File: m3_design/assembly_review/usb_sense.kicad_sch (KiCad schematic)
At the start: 3 parts

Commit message: R2 part-by-part datasheet verification; fix every issue found
All 99 BOM lines / 205 positions checked against manufacturer datasheets
(pinout, land pattern, polarity, part number, 3D orientation); record in
docs/R2_VERIFICATION.md.

Fixes:
- R134/R135: Bourns CRM2512 recommended land (2.45 x 3.7 mm pads, 7.6 mm),
  moved to keep clearance; generic 2512 land had ~45 % of the pad area.
- BOOT0 rerouted out from between the MS5611 pads (TE: do not route
  between pads); 0/45/90 segments instead of 0.1 mm staircases.
- C84 polarity mark on the top side; U12 pin-1 mark.
- AON7524 3D model rotated 180 deg; L1/L2 model height 3.0 mm.
- R84 C705743, R9 C25915, R86 80.6k 0.1% C861568 (80k not orderable);
  every BOM line now has an LCSC code.
- sim_r2: fire with all four servos stalled (FMEA V-15) passes.
- FMEA H-1..H-10 status, redundancy table, firmware requirements,
  README / STATUS / AGENTS updated for R2.

DRC 0 / unconnected 0 / parity 0 / ERC 0, audit OK, actuator contract OK;
diagnostics 173, firmware 112, quality_audit 12 tests pass; sim 135 PASS.

Co-Authored-By: Claude Opus 5.5 (1M context) <noreply@anthropic.com>
Claude-Session: https://claude.ai/code/session_01DdkfTxR7SVyv9xZNmPk9vB
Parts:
- R9: LCSC (none) -> C25915; LCSC Part (none) -> C25915; Manufacturer Yageo -> UNI-ROYAL; Manufacturer Part RC0402FR-076K2L -> 0402WGF6201TCE
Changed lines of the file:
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@@
 					(size 1.27 1.27))
 				(justify left)))
-		(property "LCSC" ""
+		(property "LCSC" "C25915"
 			(at 78.74 83.82 0)
 			(hide yes)
@@
 					(reference "R9")
 					(unit 1))))
-		(property "Manufacturer" "Yageo"
+		(property "Manufacturer" "UNI-ROYAL"
 			(at 78.74 83.82 0)
 			(hide yes)
@@
 				(font
 					(size 1.27 1.27))))
-		(property "Manufacturer Part" "RC0402FR-076K2L"
+		(property "Manufacturer Part" "0402WGF6201TCE"
 			(at 78.74 83.82 0)
 			(hide yes)
@@
 				(font
 					(size 1.27 1.27))))
-		(property "LCSC Part" ""
+		(property "LCSC Part" "C25915"
 			(at 78.74 83.82 0)
 			(hide yes)

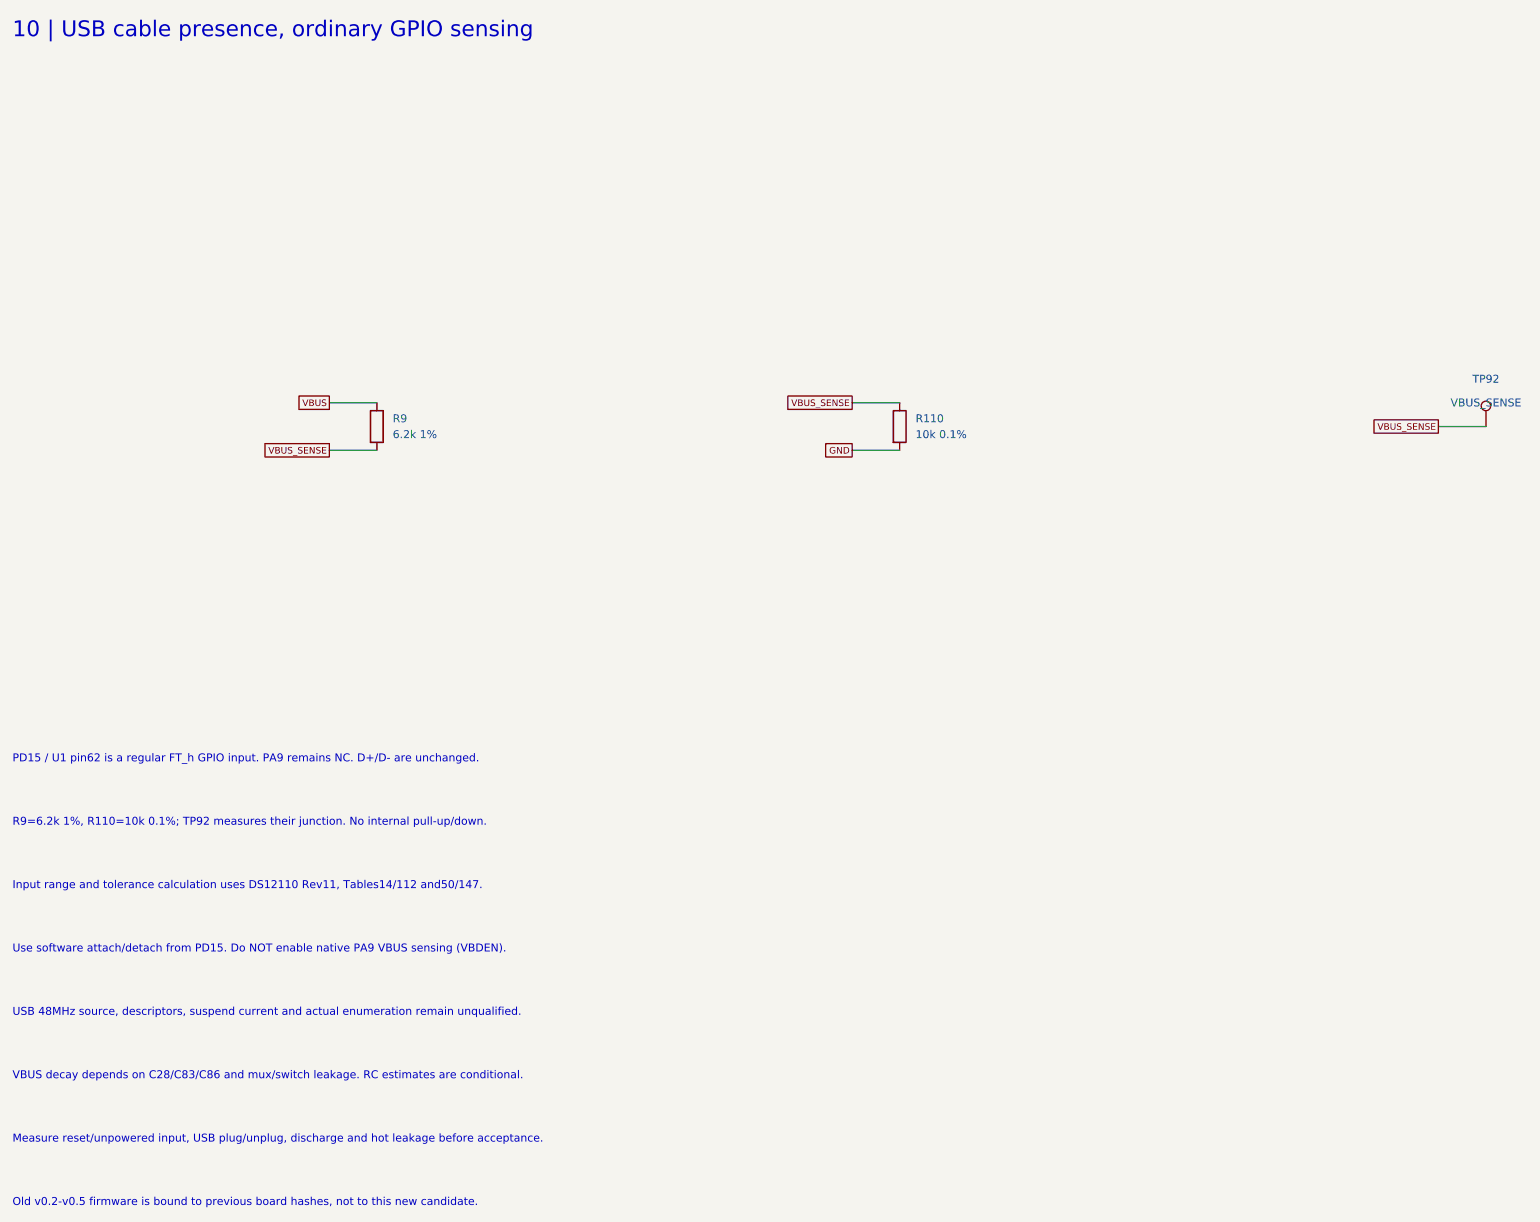
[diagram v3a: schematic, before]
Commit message: M3-ASSY-R4: R3 validation fixes, new IMU, fault-tolerant pyro sensing
The board, schematic sheets and footprint library are generated from
R3 (533af8e) by m3_design/r4_build.sh (r4_lib.py, r4_sch.py,
r4_pcb.py). docs/REQUIREMENTS.md states what the board must do;
docs/M3_R4.md records every change, the thirteen evaluation passes
(twelve independent reviews) and the accepted deviations.

- IMU: ST LSM6DSV320X (16 g and 320 g, 4000 dps)
- Pyro: black ARM and orange igniter terminals, eight pyro spacing
  rules in m3.kicad_dru, sense dividers of 2 x 5.1k over 2 x 2k in
  parallel, 4.7k at each ADC pin (R168-R172)
- Pull-pin on a JST PH connector; JLC tooling holes
- Fab: Standard PCBA, 84 BOM lines, 205 placed parts, $80.12 per board
  at five boards (tools/jlc_cost.py); placement rotations verified
- Gate: tools/check.sh DRC 0, unconnected 0, schematic parity 0, ERC 0,
  audit OK; m3_design/check_actuators.py OK

Nothing has been built or measured, and there is no R4 firmware. The
open owner decisions and the bench tests are listed in STATUS.md.

Co-Authored-By: Claude Opus 5.5 <noreply@anthropic.com>
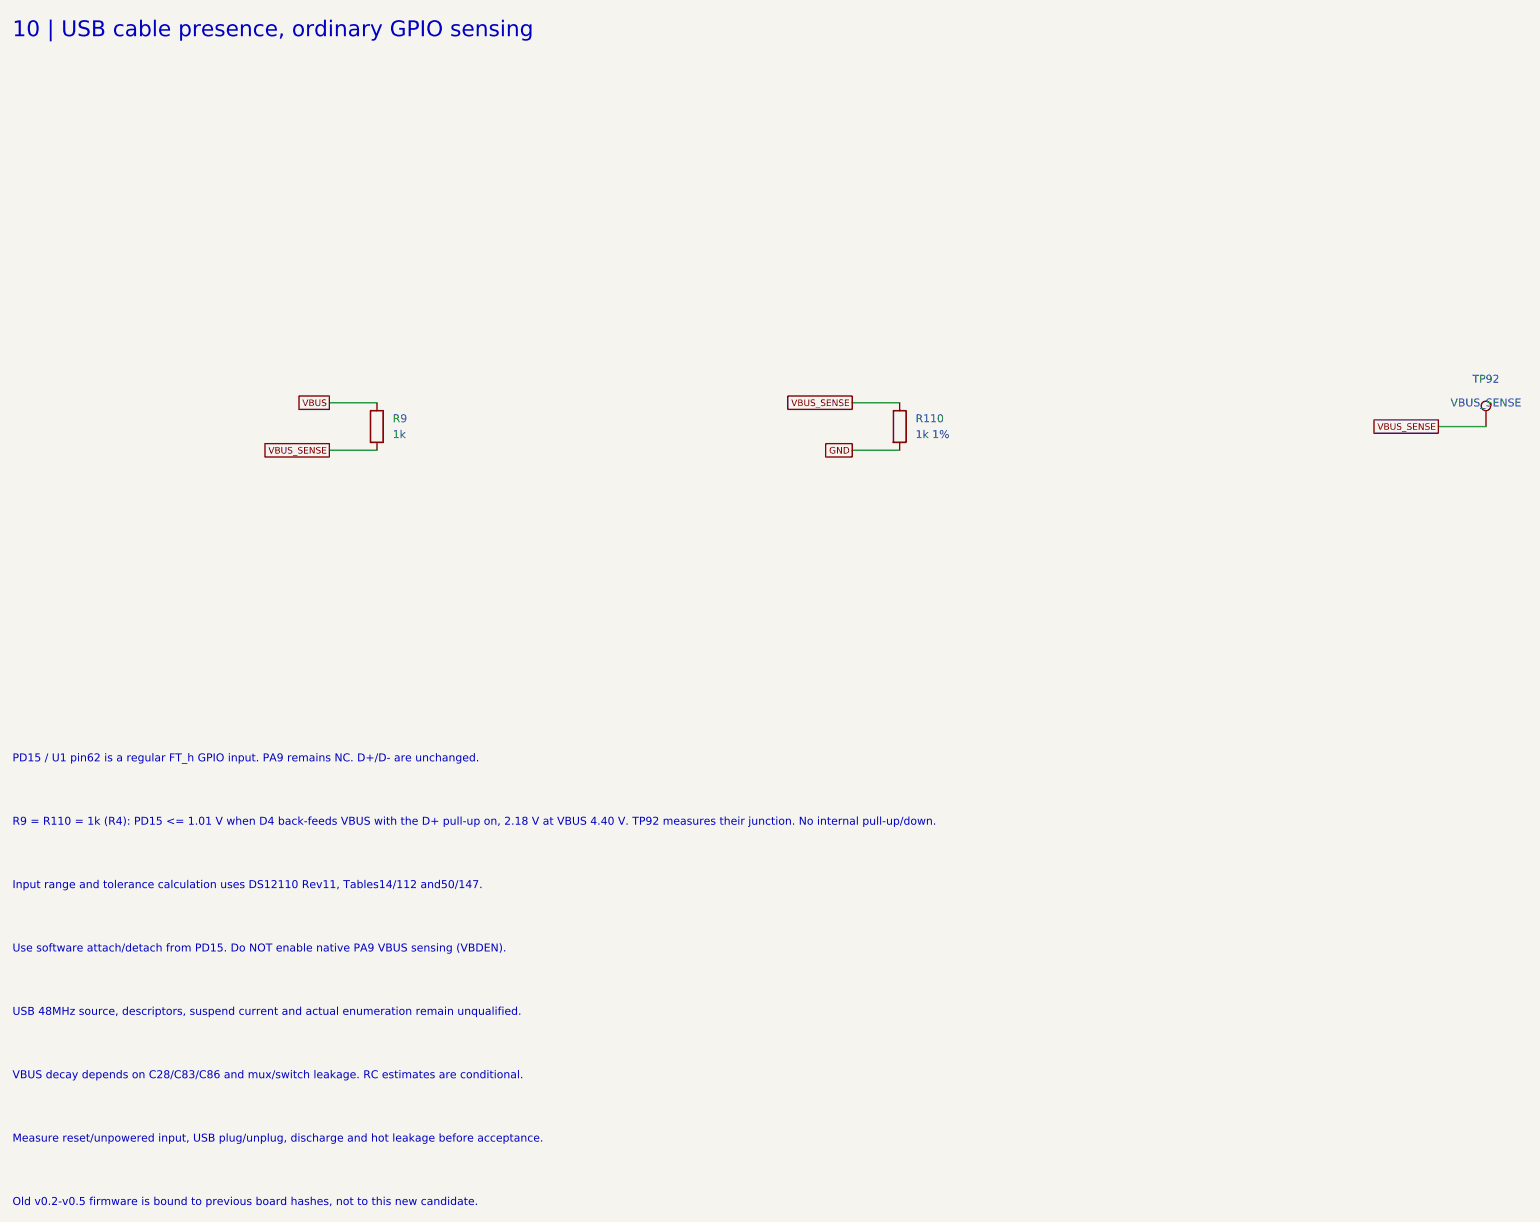
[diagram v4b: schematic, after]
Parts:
- R110: value 10k 0.1% -> 1k 1%; LCSC C95204 -> C21190; LCSC Part C95204 -> C21190; Manufacturer Yageo -> UNI-ROYAL(Uniroyal Elec); Manufacturer Part RT0603BRD0710KL -> 0603WAF1001T5E
- R9: value 6.2k 1% -> 1k; LCSC C25915 -> C11702; LCSC Part C25915 -> C11702; Manufacturer UNI-ROYAL -> (none); Manufacturer Part 0402WGF6201TCE -> (none)
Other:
- note added: "R9 = R110 = 1k (R4): PD15 <= 1.01 V when D4 back-feeds VBUS with the D+ pull-up on, 2.18 V at VBUS 4.40 V. TP92 measures their junction. No internal pull-up/down."
- note removed: "R9=6.2k 1%, R110=10k 0.1%; TP92 measures their junction. No internal pull-up/down."
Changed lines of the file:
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@@
 		(title "10 | USB cable presence, ordinary GPIO sensing")
 		(date "2026-09-07")
-		(rev "M3-ASSY-R3")
+		(rev "M3-ASSY-R4")
 		(company "Single-board M3 candidate; full system incomplete"))
 	(text "10 | USB cable presence, ordinary GPIO sensing"
@@
 					(size 1.27 1.27))
 				(justify left)))
-		(property "Value" "6.2k 1%"
+		(property "Value" "1k"
 			(at 81.28 85.09 0)
 			(effects
@@
 					(size 1.27 1.27))
 				(justify left)))
-		(property "LCSC" "C25915"
+		(property "LCSC" "C11702"
 			(at 78.74 83.82 0)
 			(hide yes)
@@
 					(reference "R9")
 					(unit 1))))
-		(property "Manufacturer" "UNI-ROYAL"
-			(at 78.74 83.82 0)
-			(hide yes)
-			(effects
-				(font
-					(size 1.27 1.27))))
-		(property "Manufacturer Part" "0402WGF6201TCE"
-			(at 78.74 83.82 0)
-			(hide yes)
-			(effects
-				(font
-					(size 1.27 1.27))))
-		(property "LCSC Part" "C25915"
+		(property "Manufacturer" ""
+			(at 78.74 83.82 0)
+			(hide yes)
+			(effects
+				(font
+					(size 1.27 1.27))))
+		(property "Manufacturer Part" ""
+			(at 78.74 83.82 0)
+			(hide yes)
+			(effects
+				(font
+					(size 1.27 1.27))))
+		(property "LCSC Part" "C11702"
 			(at 78.74 83.82 0)
 			(hide yes)
@@
 					(size 1.27 1.27))
 				(justify left)))
-		(property "Value" "10k 0.1%"
+		(property "Value" "1k 1%"
 			(at 165.1 85.09 0)
 			(effects
@@
 					(size 1.27 1.27))
 				(justify left)))
-		(property "LCSC" "C95204"
+		(property "LCSC" "C21190"
 			(at 162.56 83.82 0)
 			(hide yes)
@@
 					(reference "R110")
 					(unit 1))))
-		(property "Manufacturer" "Yageo"
-			(at 162.56 83.82 0)
-			(hide yes)
-			(effects
-				(font
-					(size 1.27 1.27))))
-		(property "Manufacturer Part" "RT0603BRD0710KL"
-			(at 162.56 83.82 0)
-			(hide yes)
-			(effects
-				(font
-					(size 1.27 1.27))))
-		(property "LCSC Part" "C95204"
+		(property "Manufacturer" "UNI-ROYAL(Uniroyal Elec)"
+			(at 162.56 83.82 0)
+			(hide yes)
+			(effects
+				(font
+					(size 1.27 1.27))))
+		(property "Manufacturer Part" "0603WAF1001T5E"
+			(at 162.56 83.82 0)
+			(hide yes)
+			(effects
+				(font
+					(size 1.27 1.27))))
+		(property "LCSC Part" "C21190"
 			(at 162.56 83.82 0)
 			(hide yes)
@@
 			(justify left))
 )
-	(text "R9=6.2k 1%, R110=10k 0.1%; TP92 measures their junction. No internal pull-up/down."
+	(text "R9 = R110 = 1k (R4): PD15 <= 1.01 V when D4 back-feeds VBUS with the D+ pull-up on, 2.18 V at VBUS 4.40 V. TP92 measures their junction. No internal pull-up/down."
 		(at 20.32 147.32 0)
 		(effects
